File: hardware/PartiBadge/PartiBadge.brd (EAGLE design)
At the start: 101.6 x 101.6 mm, 20 parts, among them J1 I2C, J2 Supply

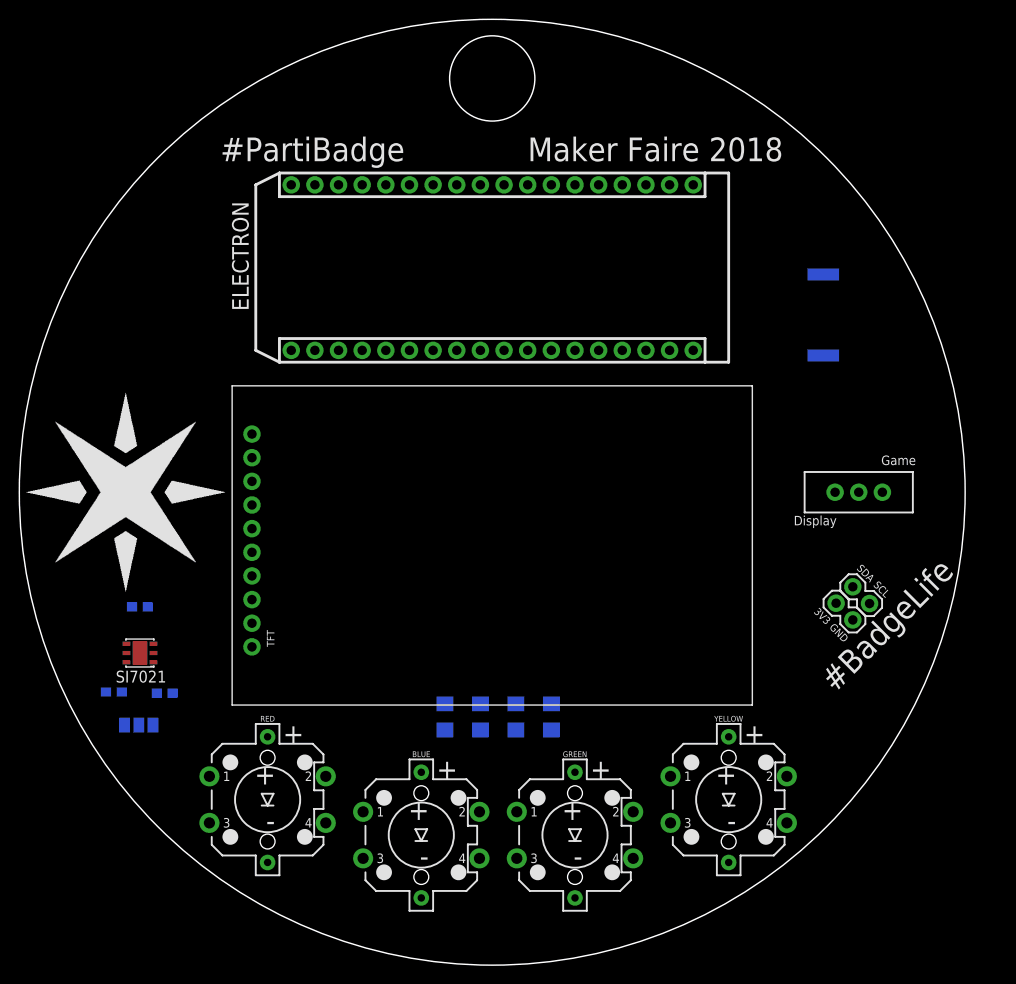
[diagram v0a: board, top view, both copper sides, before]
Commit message: increase text and add clr on piezo
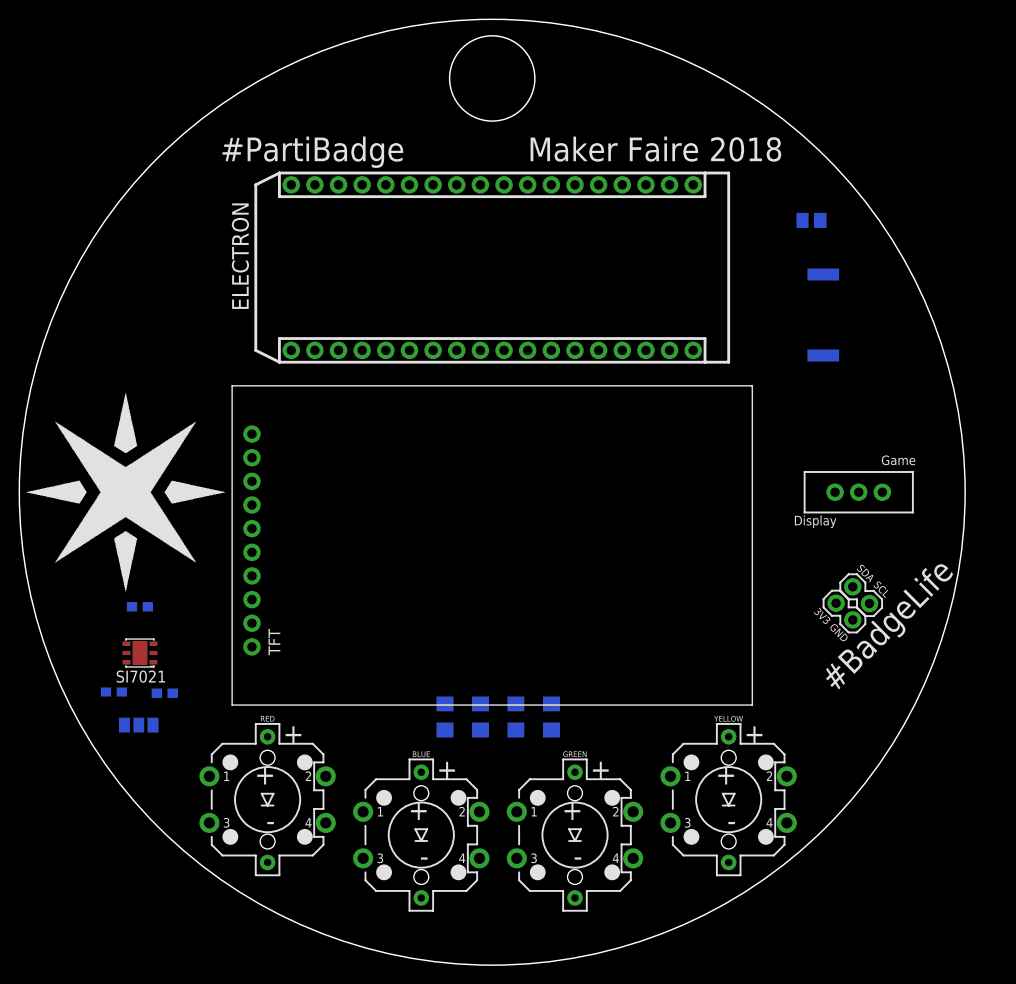
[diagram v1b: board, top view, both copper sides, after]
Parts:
- added R7: 100, rcl:M0805
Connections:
- new net N$13: PIEZO.1, R7.2
- net N$1: now also R7.1; no longer PIEZO.1
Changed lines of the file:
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@@
 <circle x="53.34" y="57.15" radius="50.8" width="0.1524" layer="20"/>
 <circle x="53.34" y="101.6" radius="4.57905" width="0.1524" layer="20"/>
-<text x="24.13" y="92.71" size="2.54" layer="21" font="vector">#PartiBadge</text>
-<text x="57.15" y="92.71" size="2.54" layer="21" font="vector">Maker Faire 2018</text>
-<text x="90.17" y="35.56" size="2.54" layer="21" font="vector" rot="R45">#BadgeLife</text>
-<text x="96.139" y="46.355" size="0.8128" layer="21" font="vector" rot="R135">SCL</text>
-<text x="94.488" y="48.006" size="0.8128" layer="21" font="vector" rot="R135">SDA</text>
-<text x="89.789" y="43.434" size="0.8128" layer="21" font="vector" rot="R135">3V3</text>
-<text x="91.694" y="41.529" size="0.8128" layer="21" font="vector" rot="R135">GND</text>
-<text x="85.725" y="53.594" size="1.016" layer="21" font="vector">Display</text>
-<text x="95.123" y="60.071" size="1.016" layer="21" font="vector">Game</text>
+<text x="24.13" y="92.71" size="2.54" layer="21" font="vector" ratio="18">#PartiBadge</text>
+<text x="57.15" y="92.71" size="2.54" layer="21" font="vector" ratio="18">Maker Faire 2018</text>
+<text x="90.17" y="35.56" size="2.54" layer="21" font="vector" ratio="18" rot="R45">#BadgeLife</text>
+<text x="96.139" y="46.355" size="0.8128" layer="21" font="vector" ratio="18" rot="R135">SCL</text>
+<text x="94.488" y="48.006" size="0.8128" layer="21" font="vector" ratio="18" rot="R135">SDA</text>
+<text x="89.789" y="43.434" size="0.8128" layer="21" font="vector" ratio="18" rot="R135">3V3</text>
+<text x="91.694" y="41.529" size="0.8128" layer="21" font="vector" ratio="18" rot="R135">GND</text>
+<text x="85.725" y="53.594" size="1.016" layer="21" font="vector" ratio="18">Display</text>
+<text x="95.123" y="60.071" size="1.016" layer="21" font="vector" ratio="18">Game</text>
 </plain>
 <attributes>
@@
 <attribute name="MF" value="Silicon Labs" x="15.494" y="39.878" size="1.778" layer="27" rot="R180" display="off"/>
 <attribute name="MPN" value="Si7021-A10-IM" x="15.494" y="39.878" size="1.778" layer="27" rot="R180" display="off"/>
-<attribute name="NAME" x="18.341" y="37.978" size="1.27" layer="25" rot="R180"/>
+<attribute name="NAME" x="18.341" y="37.978" size="1.27" layer="25" ratio="18" rot="R180"/>
 <attribute name="OC_FARNELL" value="2422573" x="15.494" y="39.878" size="1.778" layer="27" rot="R180" display="off"/>
 <attribute name="OC_NEWARK" value="55X3113" x="15.494" y="39.878" size="1.778" layer="27" rot="R180" display="off"/>
@@
 </element>
 <element name="TFT" library="SparkFun-Connectors" library_urn="urn:adsk.eagle:library:513" package="1X10_NO_SILK" package3d_urn="urn:adsk.eagle:package:38161/1" value="" x="27.5308" y="40.5384" smashed="yes" rot="R90">
-<attribute name="NAME" x="29.9438" y="40.5384" size="0.8128" layer="25" font="vector" ratio="20" rot="R90"/>
+<attribute name="NAME" x="30.5788" y="39.6494" size="1.27" layer="25" font="vector" ratio="20" rot="R90"/>
 <attribute name="PROD_ID" value="CONN-11563" x="27.5308" y="40.5384" size="1.778" layer="27" rot="R90" display="off"/>
 <attribute name="SPICEPREFIX" value="X" x="27.5308" y="40.5384" size="1.778" layer="27" rot="R90" display="off"/>
 <attribute name="VALUE" x="29.5628" y="39.2684" size="0.6096" layer="27" font="vector" ratio="20" rot="R90"/>
 </element>
-<element name="PIEZO" library="PKMCS0909E4000-R1" package="XDCR_PKMCS0909E4000-R1" value="PKMCS0909E4000-R1" x="88.9" y="76.2" rot="MR270">
+<element name="PIEZO" library="PKMCS0909E4000-R1" package="XDCR_PKMCS0909E4000-R1" value="PKMCS0909E4000-R1" x="88.9" y="76.2" smashed="yes" rot="MR270">
 <attribute name="AVAILABILITY" value="Good" x="88.9" y="76.2" size="1.778" layer="28" rot="MR270" display="off"/>
 <attribute name="DESCRIPTION" value=" Audio Sounder Piezo Solder Pad Surface Mount " x="88.9" y="76.2" size="1.778" layer="28" rot="MR270" display="off"/>
 <attribute name="MF" value="Murata" x="88.9" y="76.2" size="1.778" layer="28" rot="MR270" display="off"/>
 <attribute name="MP" value="PKMCS0909E4000-R1" x="88.9" y="76.2" size="1.778" layer="28" rot="MR270" display="off"/>
+<attribute name="NAME" x="88.093190625" y="82.993309375" size="1.27278125" layer="26" ratio="18" rot="MR180"/>
 <attribute name="PACKAGE" value="2010 Murata" x="88.9" y="76.2" size="1.778" layer="28" rot="MR270" display="off"/>
 <attribute name="PRICE" value="1.02 USD" x="88.9" y="76.2" size="1.778" layer="28" rot="MR270" display="off"/>
+<attribute name="VALUE" x="95.0794" y="80.701409375" size="1.27606875" layer="28" rot="MR270"/>
 </element>
 <element name="R1" library="SparkFun-Resistors" library_urn="urn:adsk.eagle:library:532" package="1206" package3d_urn="urn:adsk.eagle:package:39654/1" value=" 200" x="48.26" y="33.02" rot="MR270">
@@
 <element name="SJ1" library="jumper" library_urn="urn:adsk.eagle:library:252" package="SJ_2" package3d_urn="urn:adsk.eagle:package:15474/1" value="" x="15.367" y="32.131" rot="MR180"/>
 <element name="ELECTRON" library="Particle-Devices" package="ELECTRON" value="ELECTRON_WITH_HEADERS" x="27.94" y="91.44" smashed="yes" rot="R270">
-<attribute name="NAME" x="25.4" y="88.392" size="1.778" layer="25" ratio="10" rot="R270"/>
+<attribute name="NAME" x="25.4" y="88.392" size="1.778" layer="25" ratio="18" rot="R270"/>
 </element>
 <element name="YELLOW" library="SparkFun-Switches" library_urn="urn:adsk.eagle:library:535" package="TACTILE_SWITCH_LED_PTH_12MM_KIT" package3d_urn="urn:adsk.eagle:package:40174/1" value="MOMENTARY-SWITCH-SPST-LED" x="78.74" y="24.13">
@@
 <element name="J1" library="SparkFun-Connectors" library_urn="urn:adsk.eagle:library:513" package="1X02" package3d_urn="urn:adsk.eagle:package:38039/1" value="I2C" x="92.075" y="46.99" smashed="yes" rot="R315"/>
 <element name="J2" library="SparkFun-Connectors" library_urn="urn:adsk.eagle:library:513" package="1X02" package3d_urn="urn:adsk.eagle:package:38039/1" value="Supply" x="92.075" y="43.434" smashed="yes" rot="R135"/>
+<element name="R7" library="rcl" library_urn="urn:adsk.eagle:library:334" package="M0805" package3d_urn="urn:adsk.eagle:package:23556/1" value="100" x="87.63" y="86.36" rot="MR180">
+<attribute name="SPICEPREFIX" value="R" x="87.63" y="86.36" size="1.778" layer="28" rot="MR180" display="off"/>
+</element>
 </elements>
 <signals>
@@
 <wire x1="27.5308" y1="63.3984" x2="16.344" y2="44.831" width="0" layer="19" extent="16-16"/>
 </signal>
-<signal name="N$1">
-<contactref element="ELECTRON" pad="19"/>
-<contactref element="PIEZO" pad="1"/>
-<wire x1="31.75" y1="72.39" x2="88.9" y2="80.55" width="0" layer="19" extent="16-16"/>
-</signal>
 <signal name="N$2">
 <contactref element="S5" pad="1"/>
@@
 <wire x1="27.5308" y1="55.7784" x2="52.07" y2="72.39" width="0" layer="19" extent="1-1"/>
 </signal>
+<signal name="N$1">
+<contactref element="ELECTRON" pad="19"/>
+<contactref element="R7" pad="1"/>
+<wire x1="86.68" y1="86.36" x2="31.75" y2="72.39" width="0" layer="19" extent="1-1"/>
+</signal>
+<signal name="N$13">
+<contactref element="R7" pad="2"/>
+<contactref element="PIEZO" pad="1"/>
+<wire x1="88.58" y1="86.36" x2="88.9" y2="80.55" width="0" layer="19" extent="1-16"/>
+</signal>
 </signals>

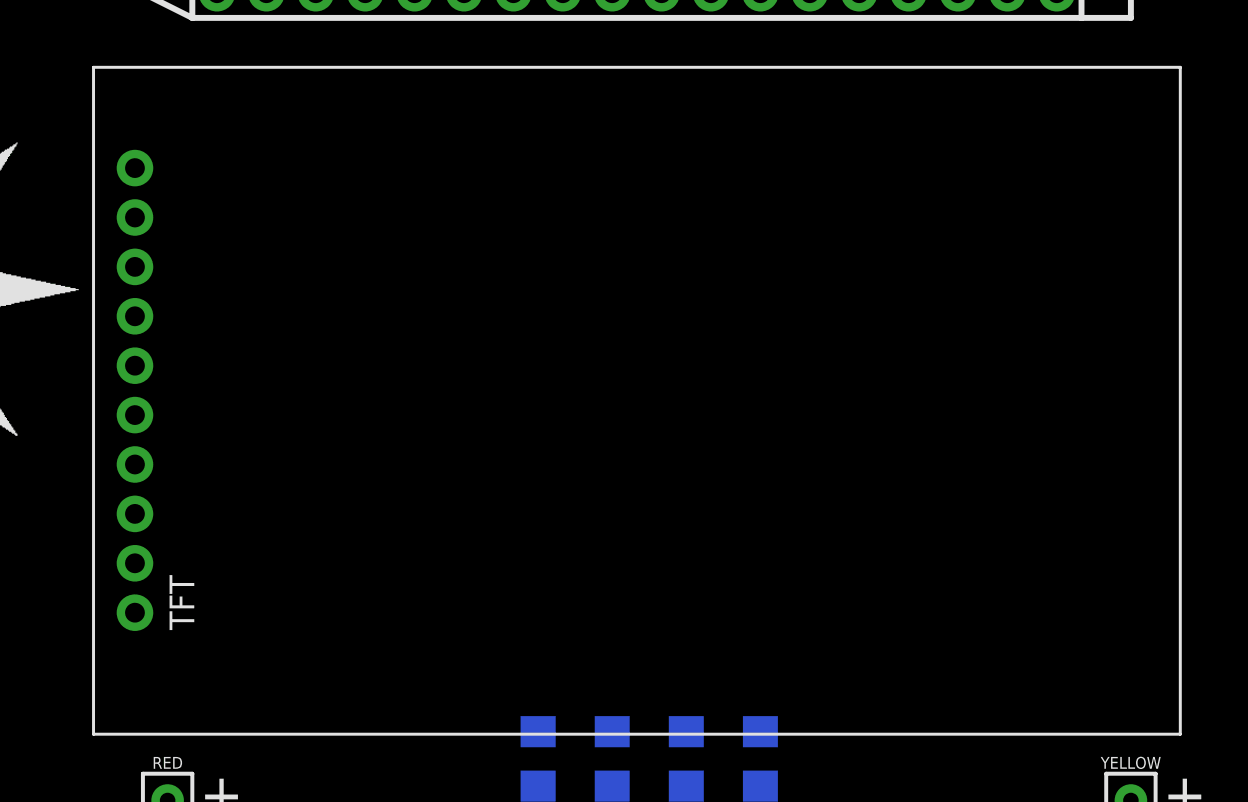
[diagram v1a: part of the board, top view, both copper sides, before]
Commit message: added tft mounting holes
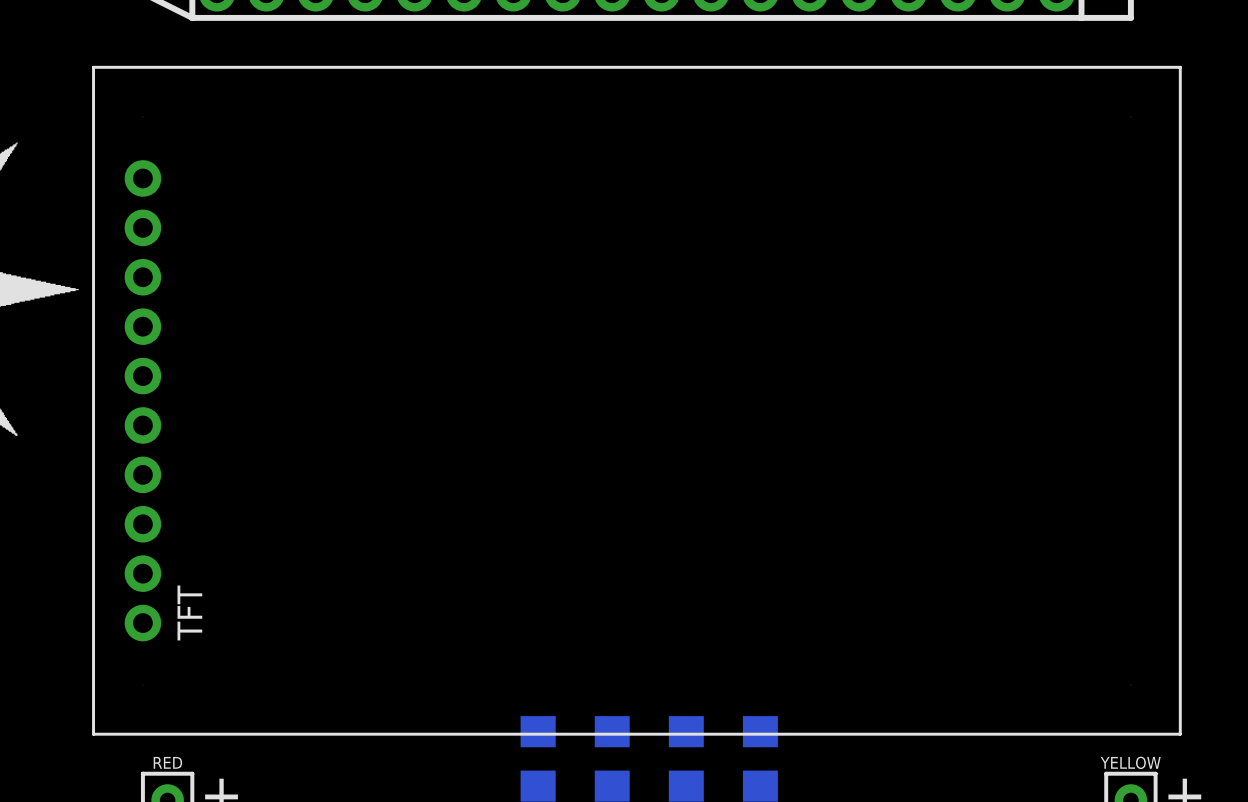
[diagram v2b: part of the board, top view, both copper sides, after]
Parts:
- moved TFT 0.67 mm to (27.9, 40.0)
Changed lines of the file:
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@@
 <drawing>
 <settings>
-<setting alwaysvectorfont="yes"/>
+<setting alwaysvectorfont="no"/>
 <setting verticaltext="up"/>
 </settings>
@@
 <layer number="43" name="vRestrict" color="2" fill="10" visible="yes" active="yes"/>
 <layer number="44" name="Drills" color="7" fill="1" visible="no" active="yes"/>
-<layer number="45" name="Holes" color="7" fill="1" visible="no" active="yes"/>
+<layer number="45" name="Holes" color="7" fill="1" visible="yes" active="yes"/>
 <layer number="46" name="Milling" color="3" fill="1" visible="no" active="yes"/>
 <layer number="47" name="Measures" color="7" fill="1" visible="no" active="yes"/>
@@
 <text x="85.725" y="53.594" size="1.016" layer="21" font="vector" ratio="18">Display</text>
 <text x="95.123" y="60.071" size="1.016" layer="21" font="vector" ratio="18">Game</text>
+<hole x="27.94" y="66.04" drill="0.0022"/>
+<hole x="78.74" y="36.83" drill="0.0022"/>
+<hole x="78.74" y="66.04" drill="0.0022"/>
+<hole x="27.94" y="36.83" drill="0.0022"/>
 </plain>
 <attributes>
@@
 <attribute name="VALUE" x="16.944" y="43.078" size="1.27" layer="27" rot="R180"/>
 </element>
-<element name="TFT" library="SparkFun-Connectors" library_urn="urn:adsk.eagle:library:513" package="1X10_NO_SILK" package3d_urn="urn:adsk.eagle:package:38161/1" value="" x="27.5308" y="40.5384" smashed="yes" rot="R90">
-<attribute name="NAME" x="30.5788" y="39.6494" size="1.27" layer="25" font="vector" ratio="20" rot="R90"/>
-<attribute name="PROD_ID" value="CONN-11563" x="27.5308" y="40.5384" size="1.778" layer="27" rot="R90" display="off"/>
-<attribute name="SPICEPREFIX" value="X" x="27.5308" y="40.5384" size="1.778" layer="27" rot="R90" display="off"/>
-<attribute name="VALUE" x="29.5628" y="39.2684" size="0.6096" layer="27" font="vector" ratio="20" rot="R90"/>
+<element name="TFT" library="SparkFun-Connectors" library_urn="urn:adsk.eagle:library:513" package="1X10_NO_SILK" package3d_urn="urn:adsk.eagle:package:38161/1" value="" x="27.94" y="40.005" smashed="yes" rot="R90">
+<attribute name="NAME" x="30.988" y="39.116" size="1.27" layer="25" font="vector" ratio="20" rot="R90"/>
+<attribute name="PROD_ID" value="CONN-11563" x="27.94" y="40.005" size="1.778" layer="27" rot="R90" display="off"/>
+<attribute name="SPICEPREFIX" value="X" x="27.94" y="40.005" size="1.778" layer="27" rot="R90" display="off"/>
+<attribute name="VALUE" x="29.972" y="38.735" size="0.6096" layer="27" font="vector" ratio="20" rot="R90"/>
 </element>
 <element name="PIEZO" library="PKMCS0909E4000-R1" package="XDCR_PKMCS0909E4000-R1" value="PKMCS0909E4000-R1" x="88.9" y="76.2" smashed="yes" rot="MR270">
@@
 <wire x1="16.944" y1="39.878" x2="29.21" y2="17.38" width="0" layer="19" extent="1-1"/>
 <wire x1="16.344" y1="44.831" x2="16.944" y2="39.878" width="0" layer="19" extent="1-16"/>
-<wire x1="27.5308" y1="63.3984" x2="16.344" y2="44.831" width="0" layer="19" extent="16-16"/>
+<wire x1="27.94" y1="62.865" x2="16.344" y2="44.831" width="0" layer="19" extent="16-16"/>
 </signal>
 <signal name="N$2">
@@
 <wire x1="90.278946875" y1="45.23005" x2="92.71" y2="57.15" width="0" layer="19" extent="1-1"/>
 <wire x1="74.93" y1="72.39" x2="92.71" y2="57.15" width="0" layer="19" extent="1-1"/>
-<wire x1="27.5308" y1="60.8584" x2="74.93" y2="72.39" width="0" layer="19" extent="1-1"/>
-<wire x1="14.644" y1="44.831" x2="27.5308" y2="60.8584" width="0" layer="19" extent="16-16"/>
+<wire x1="27.94" y1="60.325" x2="74.93" y2="72.39" width="0" layer="19" extent="1-1"/>
+<wire x1="14.644" y1="44.831" x2="27.94" y2="60.325" width="0" layer="19" extent="16-16"/>
 <wire x1="14.044" y1="39.878" x2="14.644" y2="44.831" width="0" layer="19" extent="1-16"/>
 <wire x1="15.367" y1="32.131" x2="14.044" y2="39.878" width="0" layer="19" extent="1-16"/>
@@
 <contactref element="TFT" pad="5"/>
 <contactref element="TFT" pad="6"/>
-<wire x1="27.5308" y1="53.2384" x2="52.07" y2="90.17" width="0" layer="19" extent="1-1"/>
-<wire x1="27.5308" y1="50.6984" x2="27.5308" y2="53.2384" width="0" layer="19" extent="1-1"/>
+<wire x1="27.94" y1="52.705" x2="52.07" y2="90.17" width="0" layer="19" extent="1-1"/>
+<wire x1="27.94" y1="50.165" x2="27.94" y2="52.705" width="0" layer="19" extent="1-1"/>
 </signal>
 <signal name="SPI_SCK">
 <contactref element="ELECTRON" pad="9"/>
 <contactref element="TFT" pad="3"/>
-<wire x1="27.5308" y1="45.6184" x2="54.61" y2="90.17" width="0" layer="19" extent="1-1"/>
+<wire x1="27.94" y1="45.085" x2="54.61" y2="90.17" width="0" layer="19" extent="1-1"/>
 </signal>
 <signal name="SPI_MISO">
 <contactref element="ELECTRON" pad="8"/>
 <contactref element="TFT" pad="2"/>
-<wire x1="27.5308" y1="43.0784" x2="57.15" y2="90.17" width="0" layer="19" extent="1-1"/>
+<wire x1="27.94" y1="42.545" x2="57.15" y2="90.17" width="0" layer="19" extent="1-1"/>
 </signal>
 <signal name="SPI_MOSI">
 <contactref element="ELECTRON" pad="7"/>
 <contactref element="TFT" pad="4"/>
-<wire x1="27.5308" y1="48.1584" x2="59.69" y2="90.17" width="0" layer="19" extent="1-1"/>
+<wire x1="27.94" y1="47.625" x2="59.69" y2="90.17" width="0" layer="19" extent="1-1"/>
 </signal>
 <signal name="TFT_RST">
 <contactref element="ELECTRON" pad="26"/>
 <contactref element="TFT" pad="8"/>
-<wire x1="27.5308" y1="58.3184" x2="49.53" y2="72.39" width="0" layer="19" extent="1-1"/>
+<wire x1="27.94" y1="57.785" x2="49.53" y2="72.39" width="0" layer="19" extent="1-1"/>
 </signal>
 <signal name="TFT_LITE">
 <contactref element="ELECTRON" pad="25"/>
 <contactref element="TFT" pad="1"/>
-<wire x1="27.5308" y1="40.5384" x2="46.99" y2="72.39" width="0" layer="19" extent="1-1"/>
+<wire x1="27.94" y1="40.005" x2="46.99" y2="72.39" width="0" layer="19" extent="1-1"/>
 </signal>
 <signal name="SPI_DC">
 <contactref element="ELECTRON" pad="27"/>
 <contactref element="TFT" pad="7"/>
-<wire x1="27.5308" y1="55.7784" x2="52.07" y2="72.39" width="0" layer="19" extent="1-1"/>
+<wire x1="27.94" y1="55.245" x2="52.07" y2="72.39" width="0" layer="19" extent="1-1"/>
 </signal>
 <signal name="N$1">
